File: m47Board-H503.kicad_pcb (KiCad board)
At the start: 4 copper layers, 40 x 34 mm, 44 parts, among them J1 USB_C_Receptacle_USB2.0_16P, J3 Conn_01x15_Pin, J4 Conn_01x10_Pin, J5 Conn_01x15_Pin, SW1 SW_Push, SW2 SW_Push, SW3 SW_Push, U1 AP2114H-3.3TRG1, U2 STM32H503CBTx, U3 USBLC6-2SC6, Y1 CX3225FB16000F0FZZH1 16MHz, Y2 ABS07-32.768KHZ-T

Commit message: Clean DRC
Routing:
- net +3.3V: track 31.5 -> 33.7 mm
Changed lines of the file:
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@@
 	)
 	(gr_text "m47Board-H503"
-		(at 158.35 90.7 0)
+		(at 158.35 90.5 0)
 		(layer "B.SilkS" knockout)
 		(effects
@@
 	)
 	(segment
+		(start 121.78 118.23)
+		(end 121.78 118.22)
+		(width 0.5)
+		(layer "In2.Cu")
+		(net "+3.3V")
+	)
+	(segment
+		(start 121.78 118.22)
+		(end 123.3 116.7)
+		(width 0.5)
+		(layer "In2.Cu")
+		(net "+3.3V")
+	)
+	(segment
 		(start 151.885 101.11)
 		(end 150.9 100.125)
@@
 	)
 	(segment
-		(start 142.2775 108.650988)
-		(end 142.2775 108.0225)
+		(start 141.6875 111.05)
+		(end 141.6875 109.5125)
 		(width 0.2)
 		(layer "F.Cu")
@@
 	)
 	(segment
-		(start 141.6875 111.05)
-		(end 141.6875 109.240988)
+		(start 142.2775 108.9225)
+		(end 142.2775 108.0225)
 		(width 0.2)
 		(layer "F.Cu")
@@
 	)
 	(segment
-		(start 141.6875 109.240988)
-		(end 142.2775 108.650988)
+		(start 141.6875 109.5125)
+		(end 142.2775 108.9225)
 		(width 0.2)
 		(layer "F.Cu")

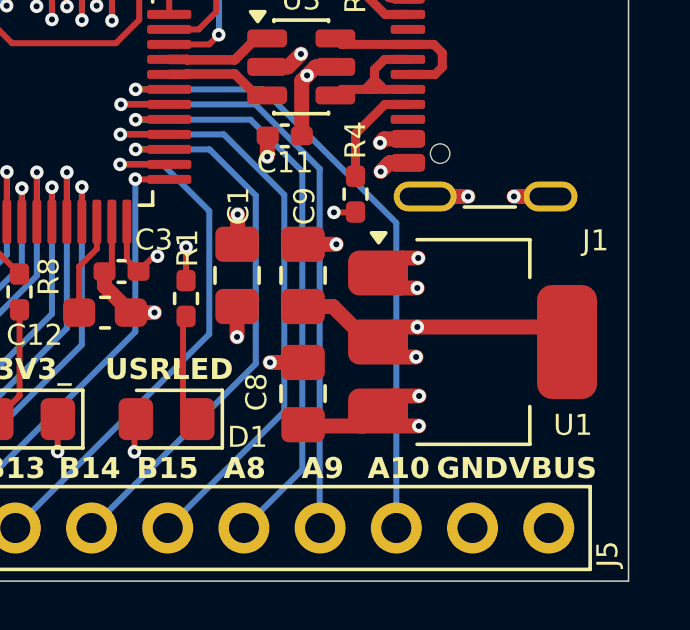
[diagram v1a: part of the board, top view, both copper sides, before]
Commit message: Swap LDO, clean DRC
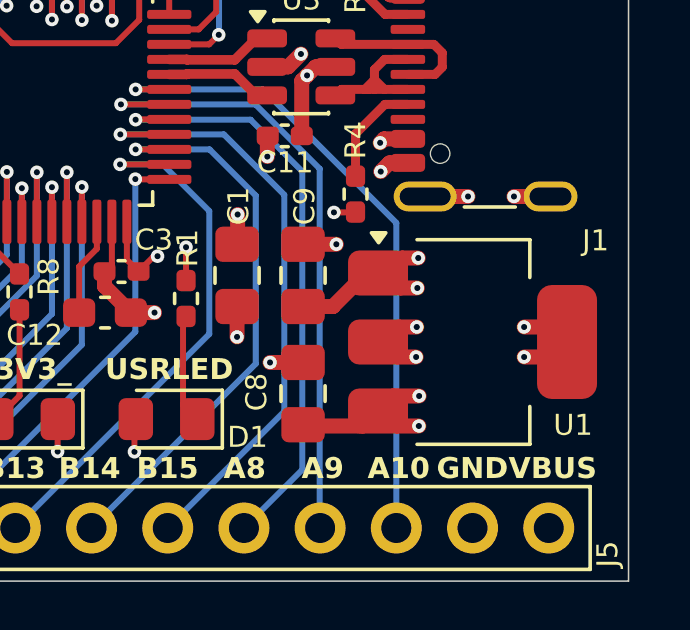
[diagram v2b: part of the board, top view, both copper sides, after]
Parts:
- U1: value AP2114H-3.3TRG1 -> AP2114HA-3.3TRG1
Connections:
- C8 pad 1: VBUS -> +3.3V
- C9 pad 1: +3.3V -> VBUS
- U1 pad 1: GND -> VBUS
- U1 pad 2: +3.3V -> GND
- U1 pad 3: VBUS -> +3.3V
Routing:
- net +3.3V: track 33.7 -> 28.4 mm
- net GND: track 56.2 -> 58.5 mm, vias 42 -> 44

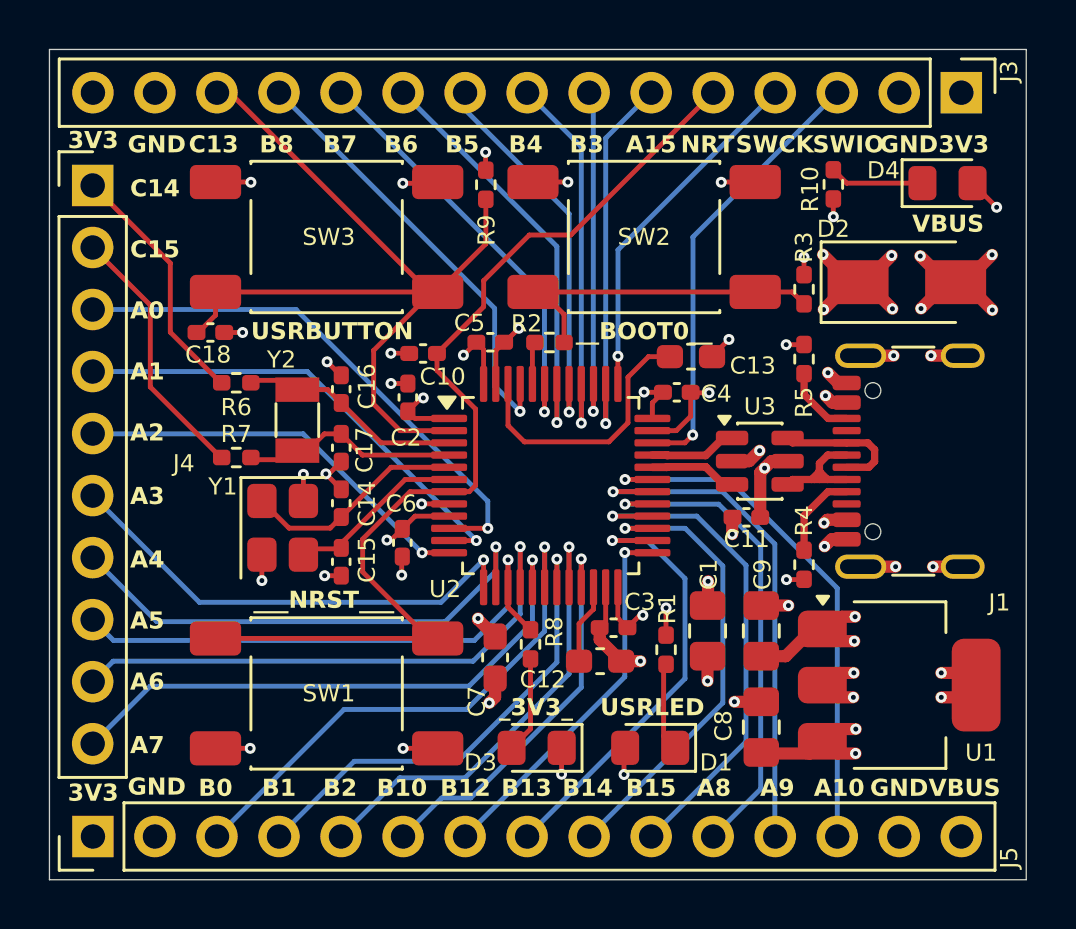
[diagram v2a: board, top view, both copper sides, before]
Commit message: Inspect before production, reroute some tracks
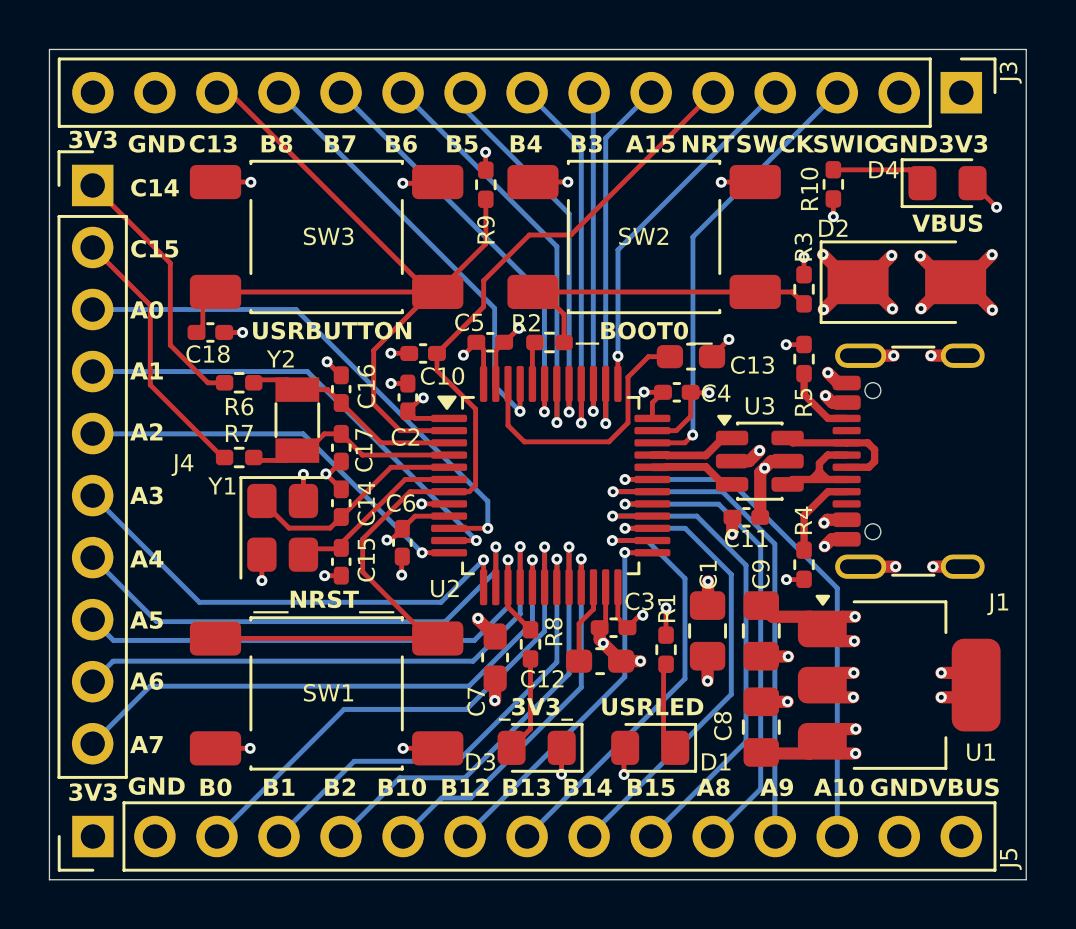
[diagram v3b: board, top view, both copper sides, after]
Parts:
- moved R6 0.12 mm to (127.8, 99.7)
- moved R7 0.12 mm to (127.8, 102.7)
- turned C9 to -90 degrees
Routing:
- net GND: track 58.5 -> 58.3 mm, vias 44 -> 45

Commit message: Add rev to silk, fill tables
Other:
- board text added: "Rev 0.0.0"
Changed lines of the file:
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@@
 	)
 	(paper "A4")
+	(title_block
+		(title "m47Board-H503")
+		(date "2026-09-05")
+		(rev "0.0.0")
+		(company "m47eus2")
+		(comment 1 "https://github.com/m47eus2/m47Board-H503")
+	)
 	(layers
 		(0 "F.Cu" signal)
@@
 		)
 	)
+	(gr_text "Rev 0.0.0"
+		(at 158.3 91.8 0)
+		(layer "B.SilkS")
+		(effects
+			(font
+				(size 0.7 0.7)
+				(thickness 0.15)
+				(bold yes)
+			)
+			(justify left bottom mirror)
+		)
+	)

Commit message: Move cap
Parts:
- moved C13 0.13 mm to (146.2, 98.7)
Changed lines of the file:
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@@
 	(footprint "Capacitor_SMD:C_0603_1608Metric_Pad1.08x0.95mm_HandSolder"
 		(layer "F.Cu")
-		(at 146.27 98.58)
+		(at 146.25 98.71)
 		(descr "Capacitor SMD 0603 (1608 Metric), square (rectangular) end terminal, IPC-7351 nominal with elongated pad for handsoldering. (Body size source: IPC-SM-782 page 76, https://www.pcb-3d.com/wordpress/wp-content/uploads/ipc-sm-782a_amendment_1_and_2.pdf)")
 		(tags "capacitor handsolder")
@@
 	)
 	(segment
-		(start 147.825 97.875)
-		(end 147.16 98.54)
+		(start 147.805 98.005)
+		(end 147.14 98.67)
 		(width 0.2)
 		(layer "F.Cu")
@@
 	)
 	(via
-		(at 147.825 97.875)
+		(at 147.805 98.005)
 		(size 0.45)
 		(drill 0.2)
@@
 	)
 	(segment
-		(start 139.45 102.07)
+		(start 138.7775 99.6975)
 		(end 138.7775 101.3975)
 		(width 0.2)
@@
 	)
 	(segment
-		(start 144.53 98.58)
-		(end 143.69 99.42)
+		(start 138.7775 101.3975)
+		(end 139.45 102.07)
 		(width 0.2)
 		(layer "F.Cu")
@@
 	)
 	(segment
-		(start 142.91 102.07)
-		(end 139.45 102.07)
+		(start 143.69 101.29)
+		(end 143.69 99.69)
 		(width 0.2)
 		(layer "F.Cu")
@@
 	)
 	(segment
-		(start 145.4075 98.58)
-		(end 144.53 98.58)
+		(start 139.45 102.07)
+		(end 142.91 102.07)
 		(width 0.2)
 		(layer "F.Cu")
@@
 	)
 	(segment
-		(start 138.7775 101.3975)
-		(end 138.7775 99.6975)
+		(start 142.91 102.07)
+		(end 143.69 101.29)
 		(width 0.2)
 		(layer "F.Cu")
@@
 	)
 	(segment
-		(start 143.69 99.42)
-		(end 143.69 101.29)
+		(start 143.69 99.69)
+		(end 144.67 98.71)
 		(width 0.2)
 		(layer "F.Cu")
@@
 	)
 	(segment
-		(start 143.69 101.29)
-		(end 142.91 102.07)
+		(start 144.67 98.71)
+		(end 145.3875 98.71)
 		(width 0.2)
 		(layer "F.Cu")

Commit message: Rearrange silk
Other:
- board text added: "_VBUS_"
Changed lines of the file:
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@@
 		)
 	)
-	(gr_text "VBUS"
-		(at 155.325 93.55 0)
+	(gr_text "_VBUS_"
+		(at 154.77 93.55 0)
 		(layer "F.SilkS" knockout)
 		(effects
